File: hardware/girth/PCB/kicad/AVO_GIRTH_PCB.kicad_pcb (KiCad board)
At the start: 4 copper layers, 65.5 x 43.5 mm, 93 parts, among them J1 USB-C 16P, J2 BATERÍA 1S, Q1 AO3401A, Q2 AO3401A, Q3 AO3401A, SW1 REED (1), SW2 REED (2), U1 BQ51013BRHLR, U2 BQ24072RGTR, U3 RT9080-33GJ5, U4 ESP32-C6-MINI-1U-N4, U5 BNO085, U6 USBLC6-2SC6, Y1 32,768 kHz 12,5 pF

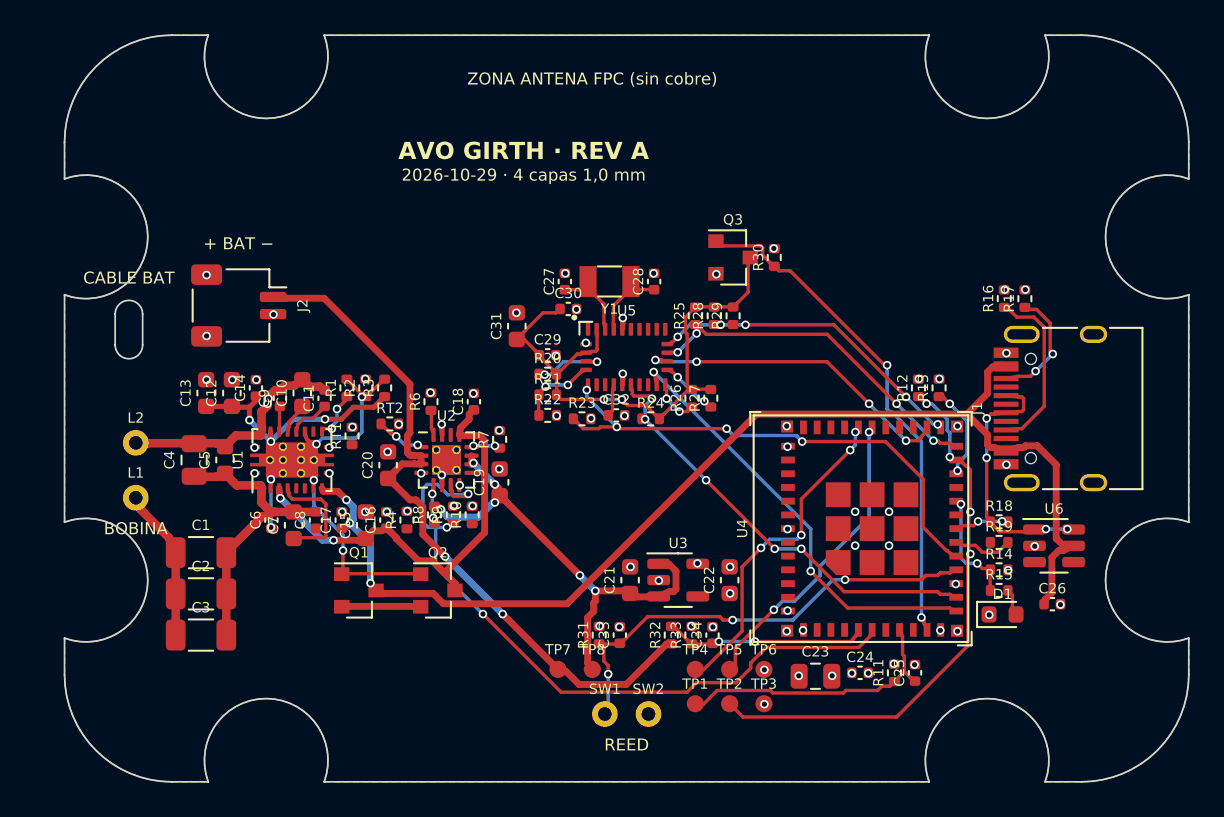
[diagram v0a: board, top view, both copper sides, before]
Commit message: PCB cincha: DRC/ERC, Gerber y renders de KiCad 9 [skip ci]
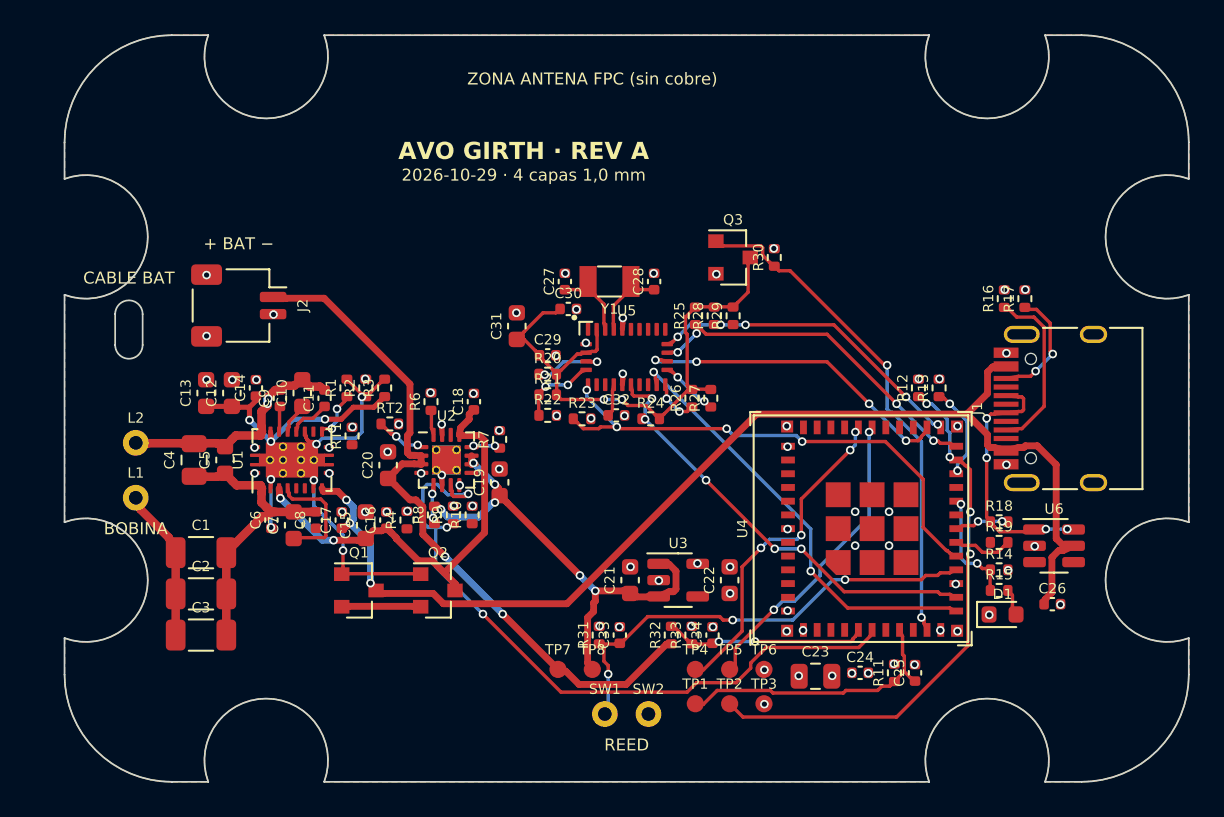
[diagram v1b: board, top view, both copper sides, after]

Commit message: PCB cincha: DRC/ERC, Gerber y renders de KiCad 9 [skip ci]
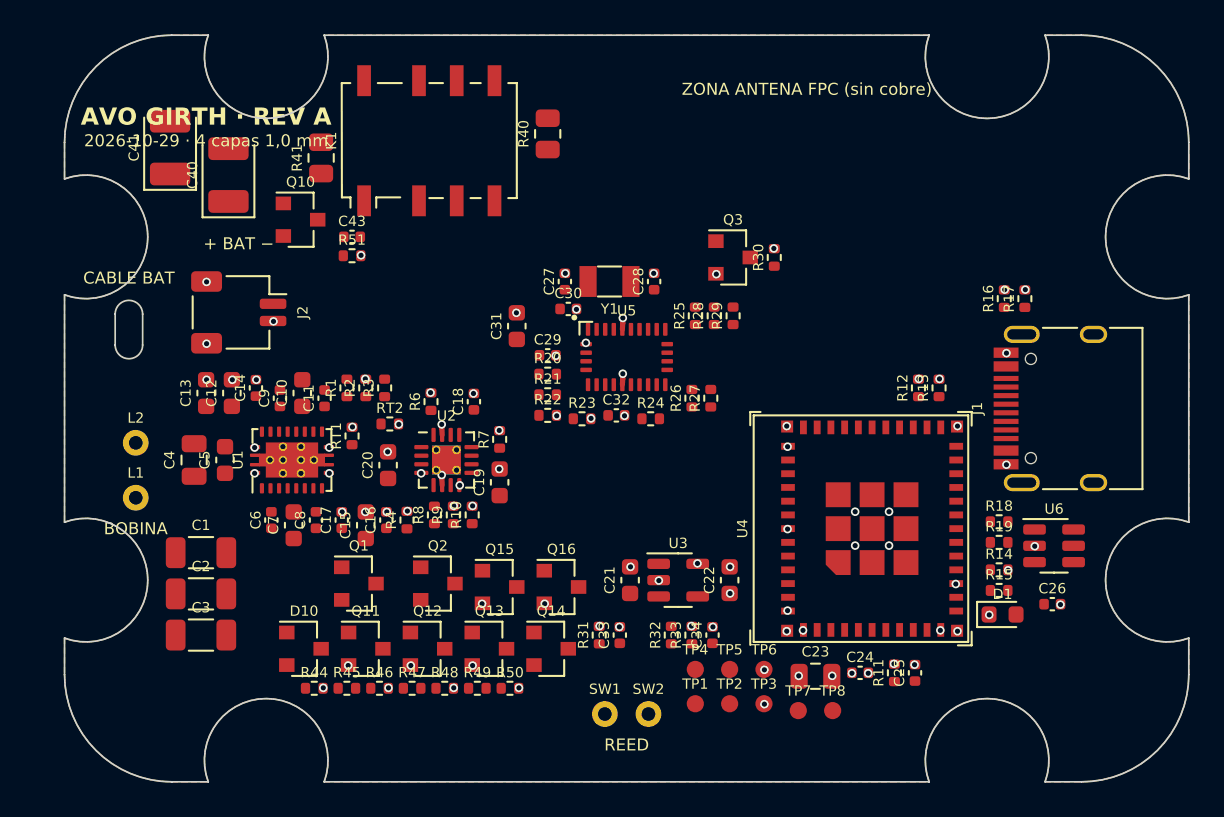
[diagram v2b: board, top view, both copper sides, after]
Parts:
- added C40: 220u 6V3 polímero, AVO:CP_EIA-3528-21_Kemet-B, F.Cu at (76.8, 86.4)
- added C41: 220u 6V3 polímero, AVO:CP_EIA-3528-21_Kemet-B, F.Cu at (73.4, 84.8)
- added C43: 100n, AVO:C_0402_1005Metric, F.Cu at (84.0, 90.0)
- added D10: BAT54C, AVO:SOT-23, F.Cu at (81.2, 114.0)
- added K1: G6KU-2F-Y DC3, AVO:Relay_DPDT_Omron_G6K-2F-Y, F.Cu at (88.5, 84.4)
- added Q10: AO3401A, AVO:SOT-23, F.Cu at (81.0, 89.0)
- added Q11: AO3400A, AVO:SOT-23, F.Cu at (84.8, 114.0)
- added Q12: 2N7002, AVO:SOT-23, F.Cu at (88.4, 114.0)
- added Q13: AO3400A, AVO:SOT-23, F.Cu at (92.0, 114.0)
- added Q14: AO3401A, AVO:SOT-23, F.Cu at (95.6, 114.0)
- added Q15: 2N7002, AVO:SOT-23, F.Cu at (92.6, 110.4)
- added Q16: 2N7002, AVO:SOT-23, F.Cu at (96.2, 110.4)
- added R40: 0R, AVO:R_0805_2012Metric, F.Cu at (95.4, 84.0)
- added R41: 0R, AVO:R_0805_2012Metric, F.Cu at (82.2, 85.4)
- added R44: 10k, AVO:R_0402_1005Metric, F.Cu at (81.8, 116.3)
- added R45: 10k, AVO:R_0402_1005Metric, F.Cu at (83.7, 116.3)
- added R46: 100k, AVO:R_0402_1005Metric, F.Cu at (85.6, 116.3)
- added R47: 100k, AVO:R_0402_1005Metric, F.Cu at (87.5, 116.3)
- added R48: 100k, AVO:R_0402_1005Metric, F.Cu at (89.4, 116.3)
- added R49: 100k, AVO:R_0402_1005Metric, F.Cu at (91.3, 116.3)
- added R50: 1M, AVO:R_0402_1005Metric, F.Cu at (93.2, 116.3)
- added R51: 1M, AVO:R_0402_1005Metric, F.Cu at (84.0, 91.1)
- R31: value 1M -> 100k
- moved TP7 14.2 mm to (110.0, 117.6)
- moved TP8 14.2 mm to (112.0, 117.6)
- moved J2 0.40 mm to (77.4, 94.4)
- moved Q1 0.40 mm to (84.4, 110.2)
- moved Q2 0.40 mm to (89.0, 110.2)
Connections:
- J2 pad 1: VBAT -> BAT_RAW
- SW1 pad 1: REED -> REED_HI
- SW2 pad 1: GND -> BAT_RAW
- U4 pad 29: (no net) -> RLY_OFF
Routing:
- net VBUS: track 68.7 -> 0.00 mm, vias 3 -> 0
- net VBAT: track 41.1 -> 0.00 mm, vias 2 -> 0
- net CHG_PG: track 41.1 -> 0.00 mm, vias 3 -> 0
- net IMU_VDD: track 32.7 -> 0.00 mm, vias 2 -> 0
- net BOOT: track 32.2 -> 0.00 mm, vias 4 -> 0
- net IMU_WAKE: track 30.5 -> 0.00 mm, vias 4 -> 0
- net IMU_PWR_N: track 29.6 -> 0.00 mm, vias 2 -> 0
- net VSYS: track 27.6 -> 0.00 mm, vias 6 -> 0
- net REED: track 27.0 -> 0.00 mm, vias 3 -> 0
- net IMU_RST: track 26.0 -> 0.00 mm, vias 5 -> 0
- net VIN5: track 25.9 -> 0.00 mm, vias 2 -> 0
- net IMU_INT: track 25.6 -> 0.00 mm, vias 2 -> 0
- net IMU_CS: track 20.8 -> 0.00 mm, vias 4 -> 0
- net IMU_SCK: track 19.3 -> 0.00 mm, vias 5 -> 0
- net U0TX: track 19.3 -> 0.00 mm, vias 4 -> 0
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
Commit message: PCB cincha: DRC/ERC, Gerber y renders de KiCad 9 [skip ci]
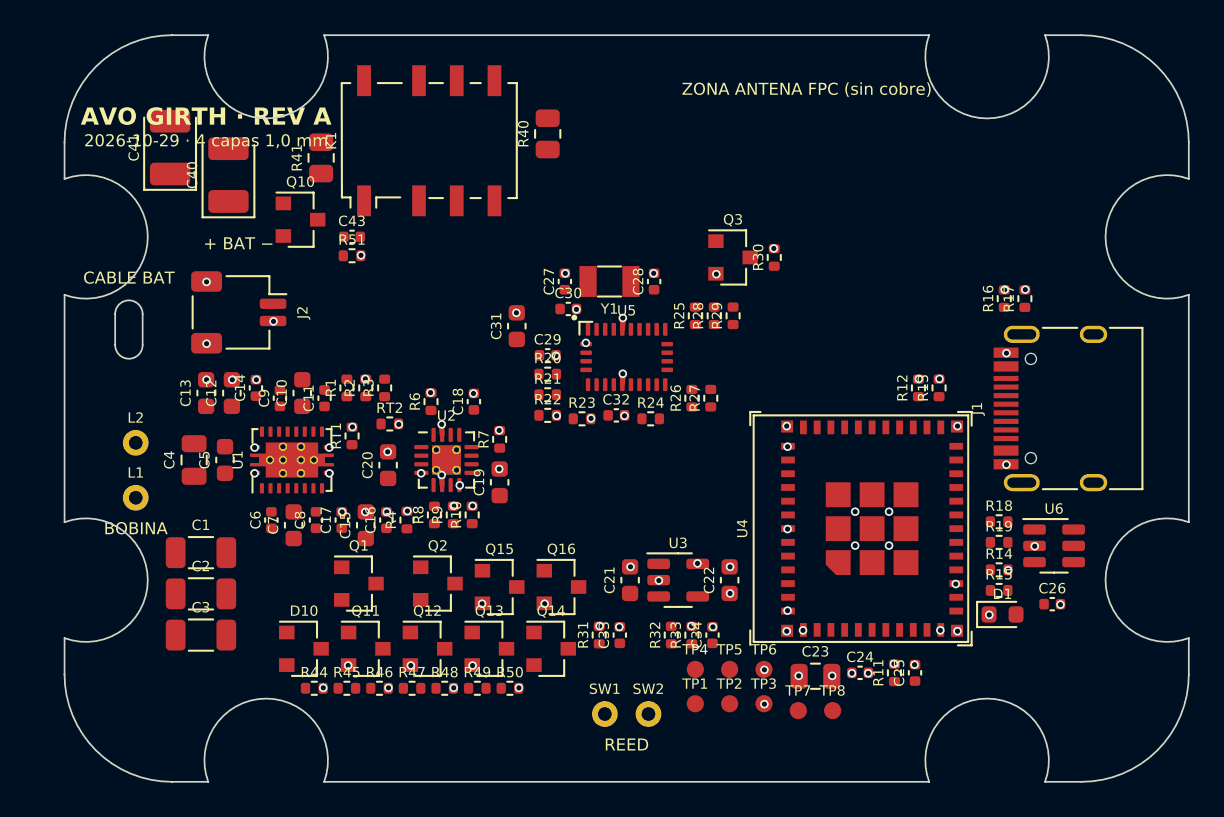
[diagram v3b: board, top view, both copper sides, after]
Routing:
- removed copper zone on B.Cu, net GND
- removed copper zone on F.Cu, net GND

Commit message: PCB cincha: DRC/ERC, Gerber y renders de KiCad 9 [skip ci]
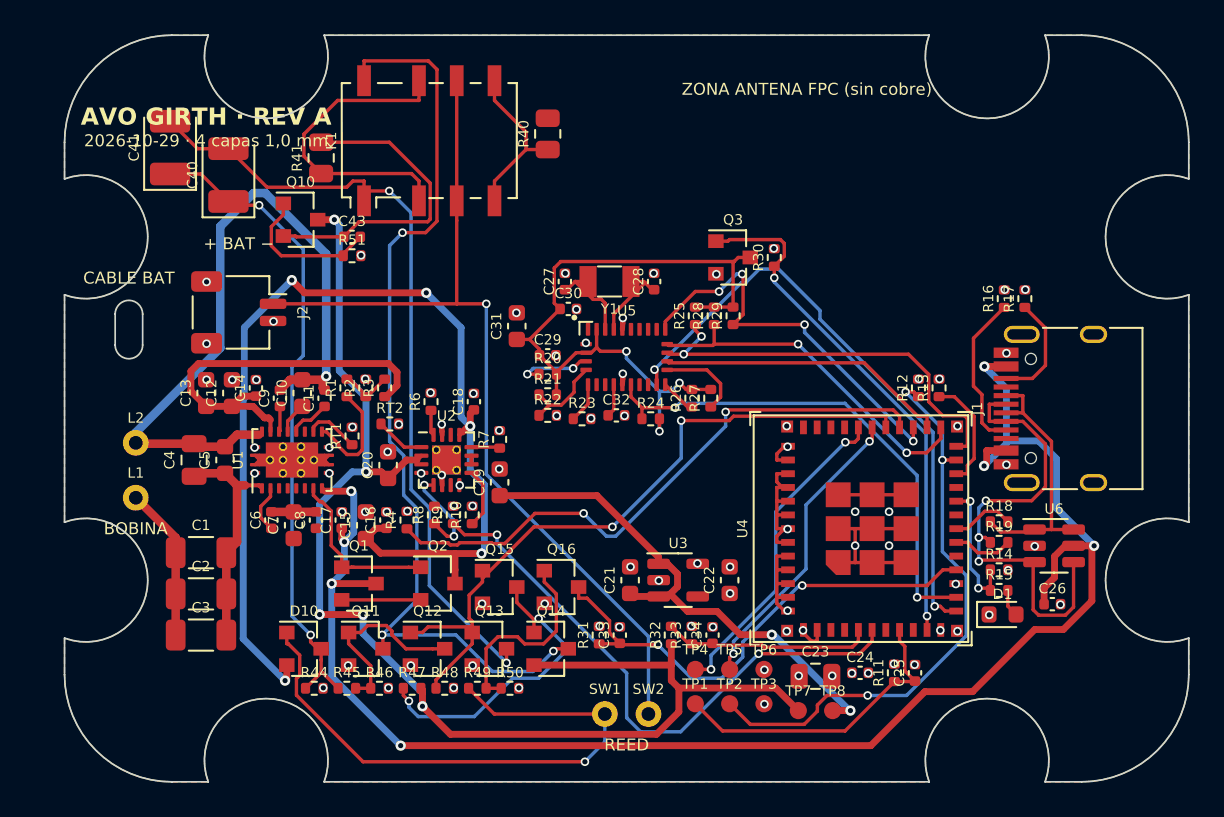
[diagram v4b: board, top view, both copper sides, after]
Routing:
- net VBUS: track 0.00 -> 94.4 mm, vias 0 -> 7
- net VBAT: track 0.00 -> 76.5 mm, vias 0 -> 5
- net VIN5: track 0.00 -> 63.5 mm, vias 0 -> 5
- net K_B: track 0.00 -> 55.1 mm, vias 0 -> 3
- net BAT_RAW: track 0.00 -> 53.2 mm, vias 0 -> 1
- net K_A: track 0.00 -> 46.8 mm, vias 0 -> 2
- net QI_AC2: track 0.00 -> 41.7 mm, vias 0 -> 1
- net IMU_VDD: track 0.00 -> 41.5 mm, vias 0 -> 3
- net RLY_OFF: track 0.00 -> 41.2 mm, vias 0 -> 2
- net RLY_P: track 0.00 -> 38.1 mm, vias 0 -> 2
- net GND: track 4.70 -> 42.1 mm
- net IMU_INT: track 0.00 -> 35.4 mm, vias 0 -> 2
- net QI_CHG: track 0.00 -> 34.8 mm, vias 0 -> 2
- net REED_HI: track 0.00 -> 34.3 mm, vias 0 -> 1
- net CHG_PG: track 0.00 -> 34.1 mm, vias 0 -> 2
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- added copper zone on B.Cu, net GND
- added copper zone on F.Cu, net GND

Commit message: PCB cincha: DRC/ERC, Gerber y renders de KiCad 9 [skip ci]
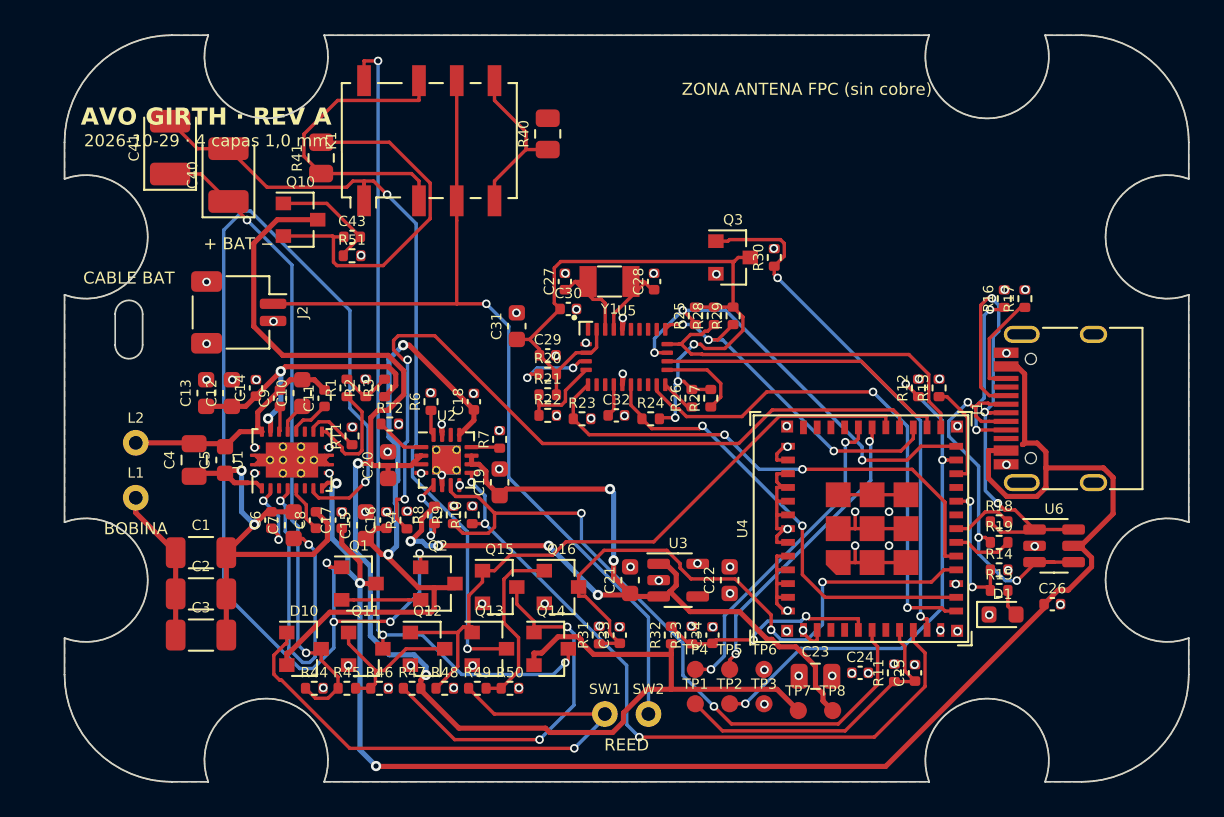
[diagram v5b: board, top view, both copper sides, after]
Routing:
- net QI_ADEN: track 9.96 -> 69.4 mm, vias 0 -> 5
- net CHG_STAT: track 3.49 -> 41.6 mm, vias 0 -> 3
- net QI_AC2: track 41.7 -> 14.0 mm, vias 1 -> 0
- net IMU_WAKE: track 2.34 -> 29.8 mm, vias 0 -> 2
- net VIN5: track 63.5 -> 40.3 mm, vias 5 -> 2
- net VSYS: track 31.1 -> 51.4 mm, vias 2 -> 6
- net QI_CLAMP1: track 0.00 -> 19.5 mm, vias 0 -> 2
- net USB_DP_C: track 15.6 -> 29.2 mm, vias 0 -> 3
- net QI_CHG: track 34.8 -> 46.1 mm
- net QI_AC1: track 16.0 -> 26.8 mm, vias 0 -> 2
- net VBAT: track 76.5 -> 83.3 mm, vias 5 -> 2
- net CHG_PG: track 34.1 -> 40.8 mm
- net K_B: track 55.1 -> 49.1 mm
- net REED: track 29.3 -> 34.9 mm
- net QI_RECT: track 23.0 -> 17.7 mm, vias 0 -> 2
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
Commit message: PCB cincha: DRC/ERC, Gerber y renders de KiCad 9 [skip ci]
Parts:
- moved C30 1.00 mm to (95.6, 94.2)
- moved R44 0.85 mm to (82.4, 116.9)
- moved R46 0.85 mm to (86.2, 116.9)
- moved R49 0.85 mm to (91.9, 116.9)
- moved R45 0.85 mm to (84.3, 116.9)
- moved R47 0.85 mm to (88.1, 116.9)
- moved R48 0.85 mm to (90.0, 116.9)
- moved R50 0.85 mm to (93.8, 116.9)
- moved C11 0.80 mm to (82.4, 98.6)
- moved C9 0.80 mm to (79.8, 98.6)
- moved C10 0.80 mm to (81.1, 98.3)
- moved C15 0.80 mm to (84.8, 107.6)
- moved C16 0.80 mm to (86.0, 107.3)
- moved C17 0.80 mm to (83.4, 107.3)
- moved C6 0.80 mm to (79.3, 107.3)
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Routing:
- net QI_ADEN: track 69.4 -> 10.9 mm, vias 5 -> 2
- net QI_CLAMP1: track 19.5 -> 0.00 mm, vias 2 -> 0
- net VSYS: track 51.4 -> 68.9 mm, vias 6 -> 5
- net USB_DP_C: track 29.2 -> 16.6 mm, vias 3 -> 0
- net RLY_PG: track 21.7 -> 12.5 mm, vias 2 -> 0
- net IMU_VDD: track 42.9 -> 51.9 mm, vias 3 -> 2
- net BAT_SW: track 21.3 -> 30.0 mm
- net QI_AC1: track 26.8 -> 18.1 mm, vias 2 -> 0
- net BAT_RAW: track 53.2 -> 60.9 mm, vias 1 -> 2
- net CHG_PG: track 40.8 -> 48.4 mm, vias 2 -> 4
- net IMU_MISO: track 20.4 -> 27.7 mm, vias 3 -> 2
- net RLY_OFF: track 39.3 -> 46.3 mm, vias 0 -> 2
- net CC1: track 9.97 -> 16.7 mm
- net IMU_CS: track 25.4 -> 32.0 mm
- net USB_DM_C: track 23.5 -> 17.3 mm, vias 3 -> 2
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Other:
- board text added: "4 capas 1,0 mm · ENIG"
- board text added: "ANTENA FPC (sin cobre)"
- board text added: "AVO GIRTH · REV A · 2026-10-29"
- board text removed: "2026-10-29 · 4 capas 1,0 mm"
- board text removed: "AVO GIRTH REV A"
- board text removed: "AVO GIRTH · REV A"
- board text removed: "CABLE BAT"
- board text removed: "ZONA ANTENA FPC (sin cobre)"
